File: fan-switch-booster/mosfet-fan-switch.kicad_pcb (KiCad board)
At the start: 2 copper layers, 50 x 62 mm, 29 parts, among them J1 12V IN, J3 FAN OUT, J4 NUC FAN HEADER, J5 FTDI HEADER, J6 ICSP, Q1 irfz44n, Q2 2n7002, Q3 irf7416, Q4 BC547, U1 Arduino_Pro_Mini_3V3

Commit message: pcb done
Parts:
- removed ? (x4): MountingHole, MountingHole:MountingHole_3.2mm_M3
- removed J6: ICSP, Connector_PinHeader_2.54mm:PinHeader_2x03_P2.54mm_Vertical
- moved C3 128.8 mm to (111.8, 89.8), turned to 90 degrees
- moved D2 127.1 mm to (94.9, 103.5)
- moved J1 123.3 mm to (95.0, 93.8), turned to 180 degrees
- moved C4 116.0 mm to (101.8, 88.2), turned to 90 degrees
- moved D3 114.5 mm to (100.2, 98.8)
- moved D1 103.3 mm to (101.7, 93.8)
- moved R3 101.2 mm to (108.2, 82.0)
- moved R4 99.7 mm to (108.0, 78.5), turned to 180 degrees
- moved Q3 98.7 mm to (109.3, 73.1), turned to 180 degrees
- moved J3 94.5 mm to (117.8, 89.8), turned to 0 degrees
- moved Q2 88.8 mm to (64.2, 91.9), turned to -90 degrees
- moved R9 83.4 mm to (86.8, 58.2), turned to 180 degrees
- moved Q1 80.4 mm to (109.8, 63.2), turned to 180 degrees
- moved R5 80.2 mm to (95.2, 78.4), turned to -90 degrees
- moved C6 76.2 mm to (96.0, 61.0), turned to 0 degrees
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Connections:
- J4 pad 3: (no net) -> unconnected-(J4-Pin_3-Pad3)
- R3 pad 1: /BOOT -> /P12V
- R3 pad 2: /P12V -> /BOOT
- U1 pad 1: (no net) -> unconnected-(U1-TX0-Pad1)
- U1 pad 10: (no net) -> unconnected-(U1-D7-Pad10)
- U1 pad 11: (no net) -> unconnected-(U1-D8-Pad11)
- U1 pad 14: (no net) -> /GND
- U1 pad 17: (no net) -> unconnected-(U1-A3-Pad17)
- U1 pad 18: (no net) -> unconnected-(U1-A2-Pad18)
- U1 pad 19: (no net) -> unconnected-(U1-A1-Pad19)
- U1 pad 2: (no net) -> unconnected-(U1-RX1-Pad2)
- U1 pad 32: (no net) -> unconnected-(U1-A6-Pad32)
- U1 pad 33: (no net) -> unconnected-(U1-A7-Pad33)
- U1 pad 34: (no net) -> unconnected-(U1-A4-Pad34)
- U1 pad 35: (no net) -> unconnected-(U1-A5-Pad35)
- U1 pad 5: (no net) -> unconnected-(U1-D2-Pad5)
- U1 pad 6: (no net) -> unconnected-(U1-D3-Pad6)
- U1 pad 7: (no net) -> unconnected-(U1-D4-Pad7)
- U1 pad 8: (no net) -> unconnected-(U1-D5-Pad8)
- U1 pad 9: (no net) -> unconnected-(U1-D6-Pad9)
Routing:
- net /GND: track 0.00 -> 187.3 mm
- net /DRAIN: track 0.00 -> 90.4 mm
- net /BOOT: track 0.00 -> 88.7 mm, vias 0 -> 2
- net /P12V: track 0.00 -> 87.8 mm
- net /RST: track 0.00 -> 42.6 mm
- net /DEMAND: track 0.00 -> 33.9 mm
- net /NUC_TACH: track 0.00 -> 32.1 mm
- net /GATE: track 0.00 -> 24.3 mm
- net /P3V3: track 0.00 -> 21.6 mm
- net /LGATE: track 0.00 -> 19.7 mm
- net /DTR: track 0.00 -> 8.94 mm
- net /TX0: track 0.00 -> 8.73 mm
- net /RX1: track 0.00 -> 8.73 mm
- net /BLK: track 0.00 -> 8.73 mm
- net /NUC_PWM: track 0.00 -> 8.52 mm
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- removed copper zone on B.Cu, net /GND
- removed copper zone on F.Cu, net /P12V
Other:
- board outline removed
- board text removed: "+12V IN"
- board text removed: "12V FAN DRIVER"
- board text removed: "3 x 100 mA"
- board text removed: "D1 K +12V"
- board text removed: "D2 D3 spare"
- board text removed: "FAN OUT"
- board text removed: "ICSP: no 5V wire"
- board text removed: "J5: 1=DTR 6=BLK"
- board text removed: "NUC FAN HEADER"
- board text removed: "NUC INTERFACE"
- board text removed: "PRO MINI 328 SOCKET"
- board text removed: "Q1 G-D-S"
- board text removed: "gnd plane on back"

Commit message: pcb manually designed
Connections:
- U1 pad 21: /SCK -> unconnected-(U1-D13-Pad21)
- U1 pad 22: /MISO -> unconnected-(U1-D12-Pad22)
- U1 pad 23: /MOSI -> unconnected-(U1-D11-Pad23)
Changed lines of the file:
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@@
 			(layers "*.Cu" "*.Mask")
 			(remove_unused_layers no)
-			(net "/SCK")
+			(net "unconnected-(U1-D13-Pad21)")
 			(pinfunction "D13_21")
-			(pintype "passive")
+			(pintype "passive+no_connect")
 		)
 		(pad "22" thru_hole circle
@@
 			(layers "*.Cu" "*.Mask")
 			(remove_unused_layers no)
-			(net "/MISO")
+			(net "unconnected-(U1-D12-Pad22)")
 			(pinfunction "D12_22")
-			(pintype "passive")
+			(pintype "passive+no_connect")
 		)
 		(pad "23" thru_hole circle
@@
 			(layers "*.Cu" "*.Mask")
 			(remove_unused_layers no)
-			(net "/MOSI")
+			(net "unconnected-(U1-D11-Pad23)")
 			(pinfunction "D11_23")
-			(pintype "passive")
+			(pintype "passive+no_connect")
 		)
 		(pad "24" thru_hole circle

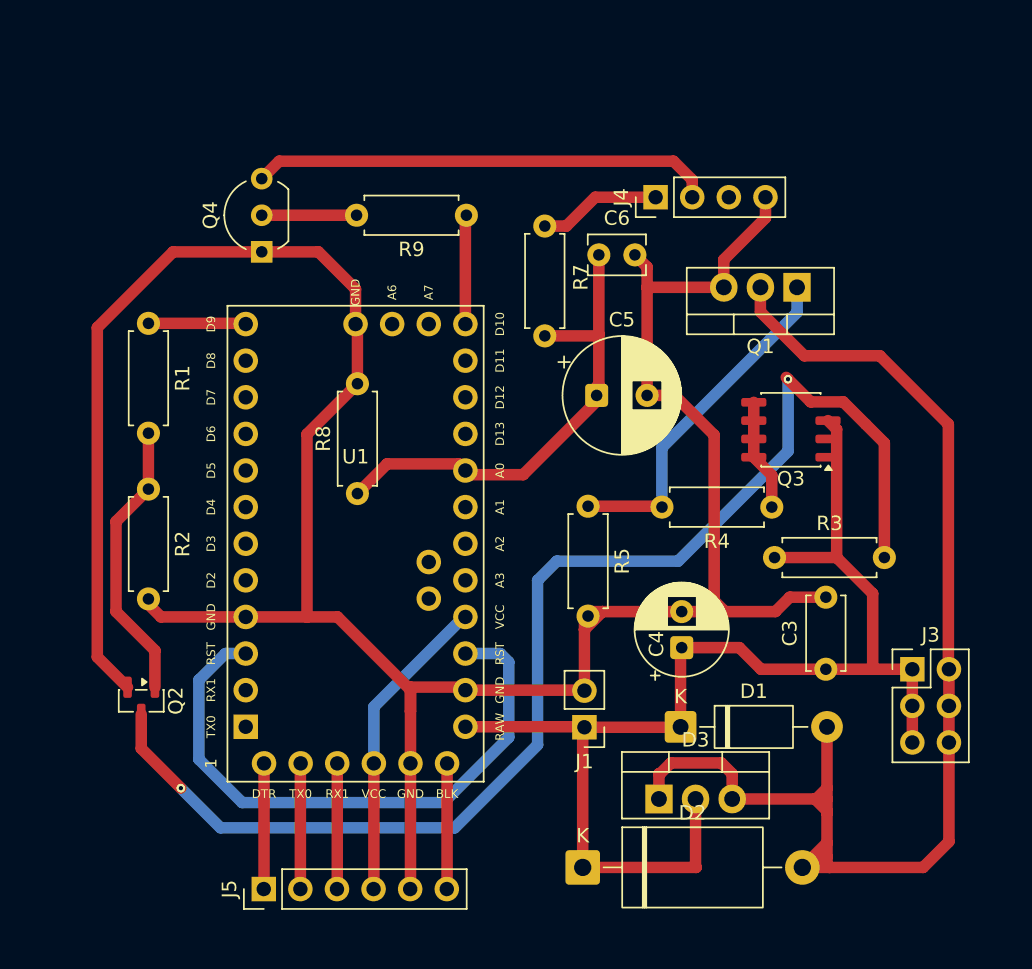
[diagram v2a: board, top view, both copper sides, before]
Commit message: pcb: edge cuts outline, four M3 holes, GND pour on F.Cu
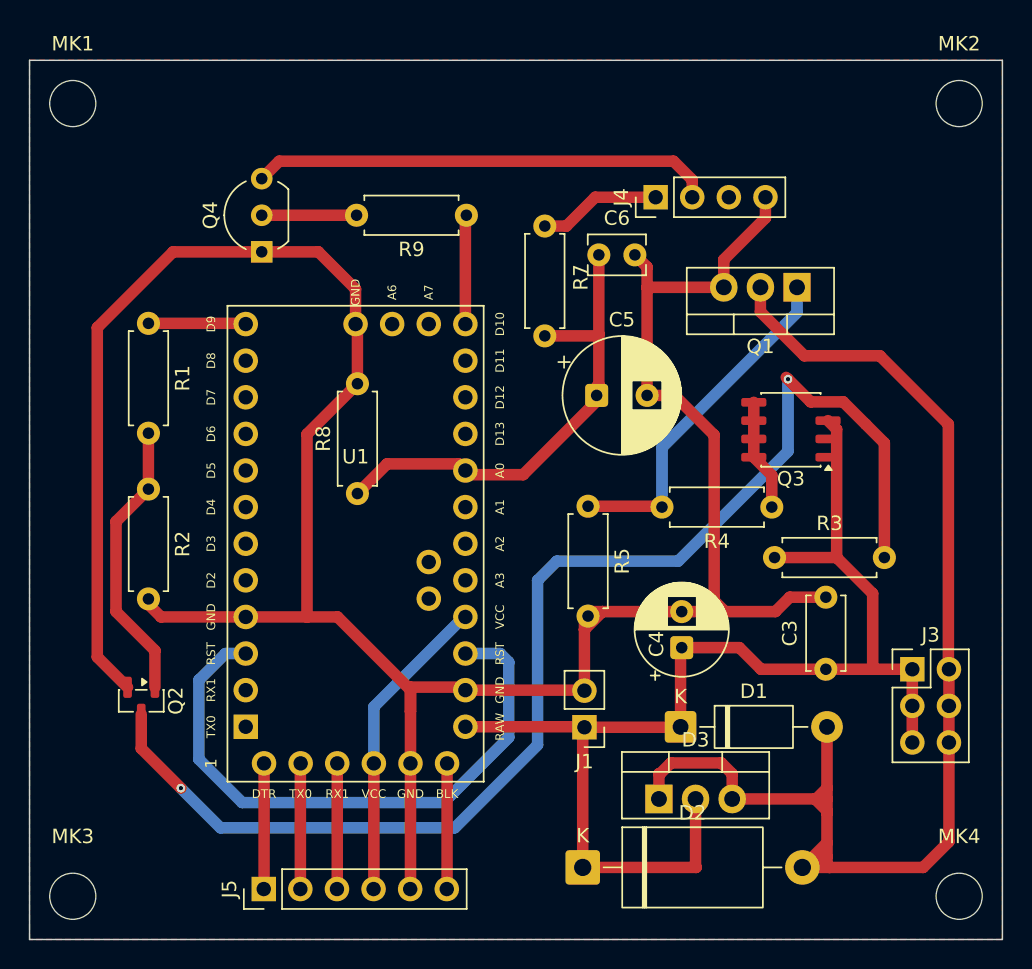
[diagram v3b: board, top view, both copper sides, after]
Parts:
- added MK1: M3 mounting hole, MountingHole:MountingHole_3.2mm_M3, F.Cu at (59.5, 50.5)
- added MK2: M3 mounting hole, MountingHole:MountingHole_3.2mm_M3, F.Cu at (121.0, 50.5)
- added MK3: M3 mounting hole, MountingHole:MountingHole_3.2mm_M3, F.Cu at (59.5, 105.5)
- added MK4: M3 mounting hole, MountingHole:MountingHole_3.2mm_M3, F.Cu at (121.0, 105.5)
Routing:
- added copper zone on F.Cu, net /GND
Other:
- board outline added: 67.5 x 61 mm

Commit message: pcb: compact outline to 63.2 x 54.4 mm, four M3 holes at the corners
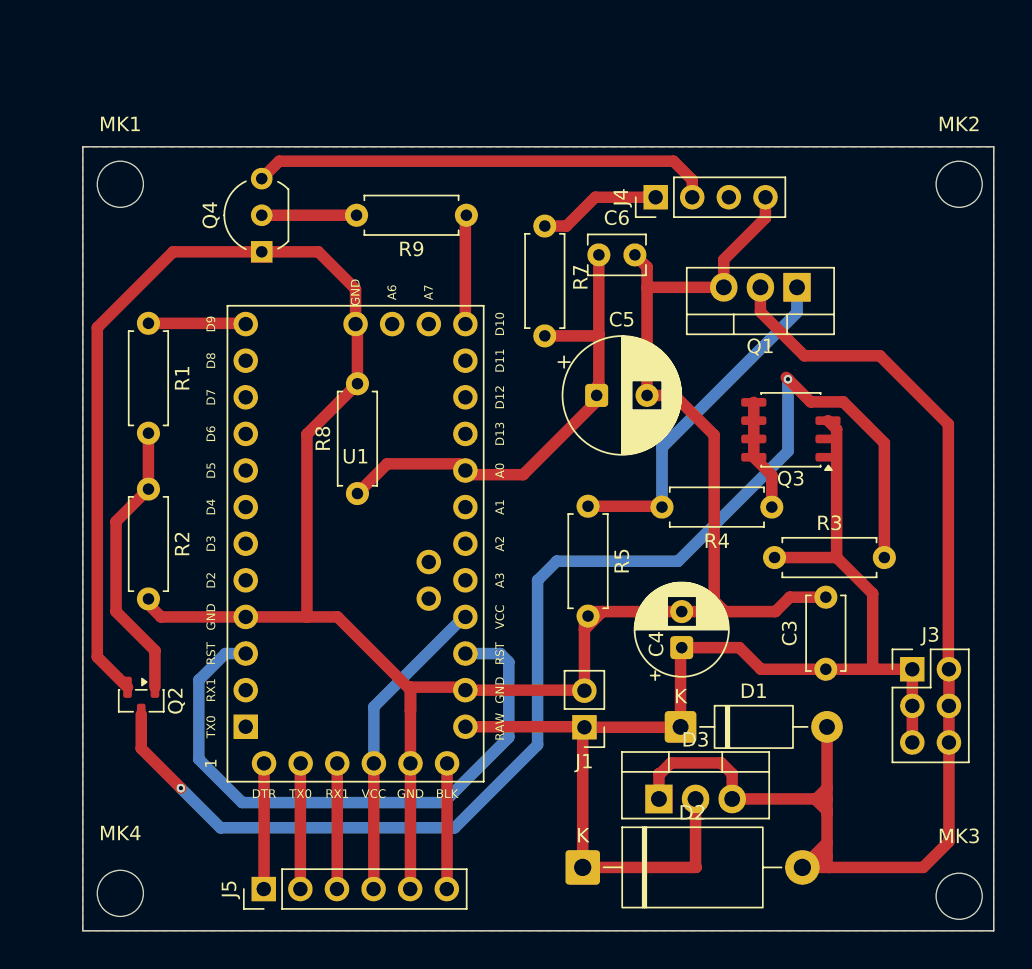
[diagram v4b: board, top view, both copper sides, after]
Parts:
- moved MK3 61.5 mm to (121.0, 105.5)
- moved MK4 58.2 mm to (62.8, 105.3)
- moved MK1 6.50 mm to (62.8, 56.1)
- moved MK2 5.60 mm to (121.0, 56.1)
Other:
- board size 67.5 x 61 mm -> 63.2 x 54.4 mm
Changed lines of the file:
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@@
 	(footprint "MountingHole:MountingHole_3.2mm_M3"
 		(layer "F.Cu")
-		(at 121 105.5)
+		(at 62.8 105.3)
 		(descr "Mounting Hole 3.2mm, M3, no annular, generated by kicad-footprint-generator mountinghole.py")
 		(tags "mountinghole M3")
@@
 	(footprint "MountingHole:MountingHole_3.2mm_M3"
 		(layer "F.Cu")
-		(at 59.5 105.5)
+		(at 121 105.5)
 		(descr "Mounting Hole 3.2mm, M3, no annular, generated by kicad-footprint-generator mountinghole.py")
 		(tags "mountinghole M3")
@@
 	(footprint "MountingHole:MountingHole_3.2mm_M3"
 		(layer "F.Cu")
-		(at 59.5 50.5)
+		(at 62.8 56.1)
 		(descr "Mounting Hole 3.2mm, M3, no annular, generated by kicad-footprint-generator mountinghole.py")
 		(tags "mountinghole M3")
@@
 	(footprint "MountingHole:MountingHole_3.2mm_M3"
 		(layer "F.Cu")
-		(at 121 50.5)
+		(at 121 56.1)
 		(descr "Mounting Hole 3.2mm, M3, no annular, generated by kicad-footprint-generator mountinghole.py")
 		(tags "mountinghole M3")
@@
 	)
 	(gr_line
-		(start 56.5 47.5)
-		(end 124 47.5)
+		(start 60.2 53.5)
+		(end 123.4 53.5)
 		(stroke
 			(width 0.1)
@@
 	)
 	(gr_line
-		(start 56.5 108.5)
-		(end 56.5 47.5)
+		(start 60.2 107.9)
+		(end 60.2 53.5)
 		(stroke
 			(width 0.1)
@@
 	)
 	(gr_line
-		(start 124 47.5)
-		(end 124 108.5)
+		(start 123.4 53.5)
+		(end 123.4 107.9)
 		(stroke
 			(width 0.1)
@@
 	)
 	(gr_line
-		(start 124 108.5)
-		(end 56.5 108.5)
+		(start 123.4 107.9)
+		(end 60.2 107.9)
 		(stroke
 			(width 0.1)
@@
 		(polygon
 			(pts
-				(xy 56.5 47.5) (xy 124 47.5) (xy 124 108.5) (xy 56.5 108.5)
+				(xy 60.2 53.5) (xy 123.4 53.5) (xy 123.4 107.9) (xy 60.2 107.9)
 			)
 		)
